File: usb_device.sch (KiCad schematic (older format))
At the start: 9 parts, among them J4 USB_C_Receptacle, U7 USB6B1, U8 USB6B1

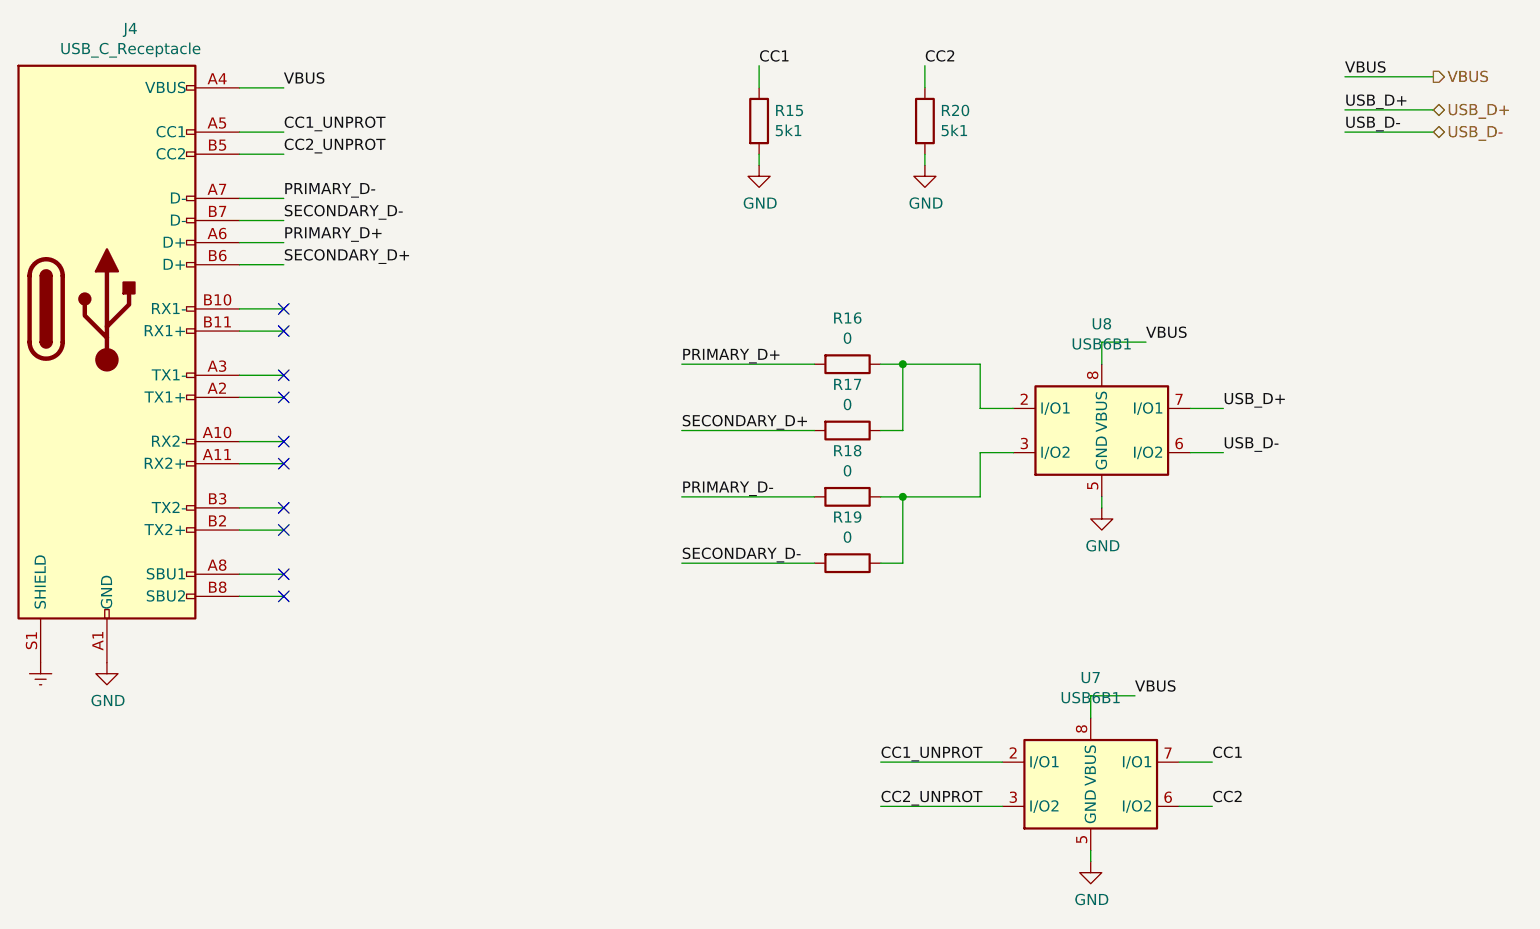
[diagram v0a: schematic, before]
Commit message: Complete muxing and level translation
Added Aux USB to avoid using a HUB, which don't seem to be too readily
available out there and would complicate the design for no good reason.

Now the i2c lines can also be switched.

Added voltage level translation up to 1.2V from 3.3V. Selected
bidirectional level translator.

Started looking into power supply.
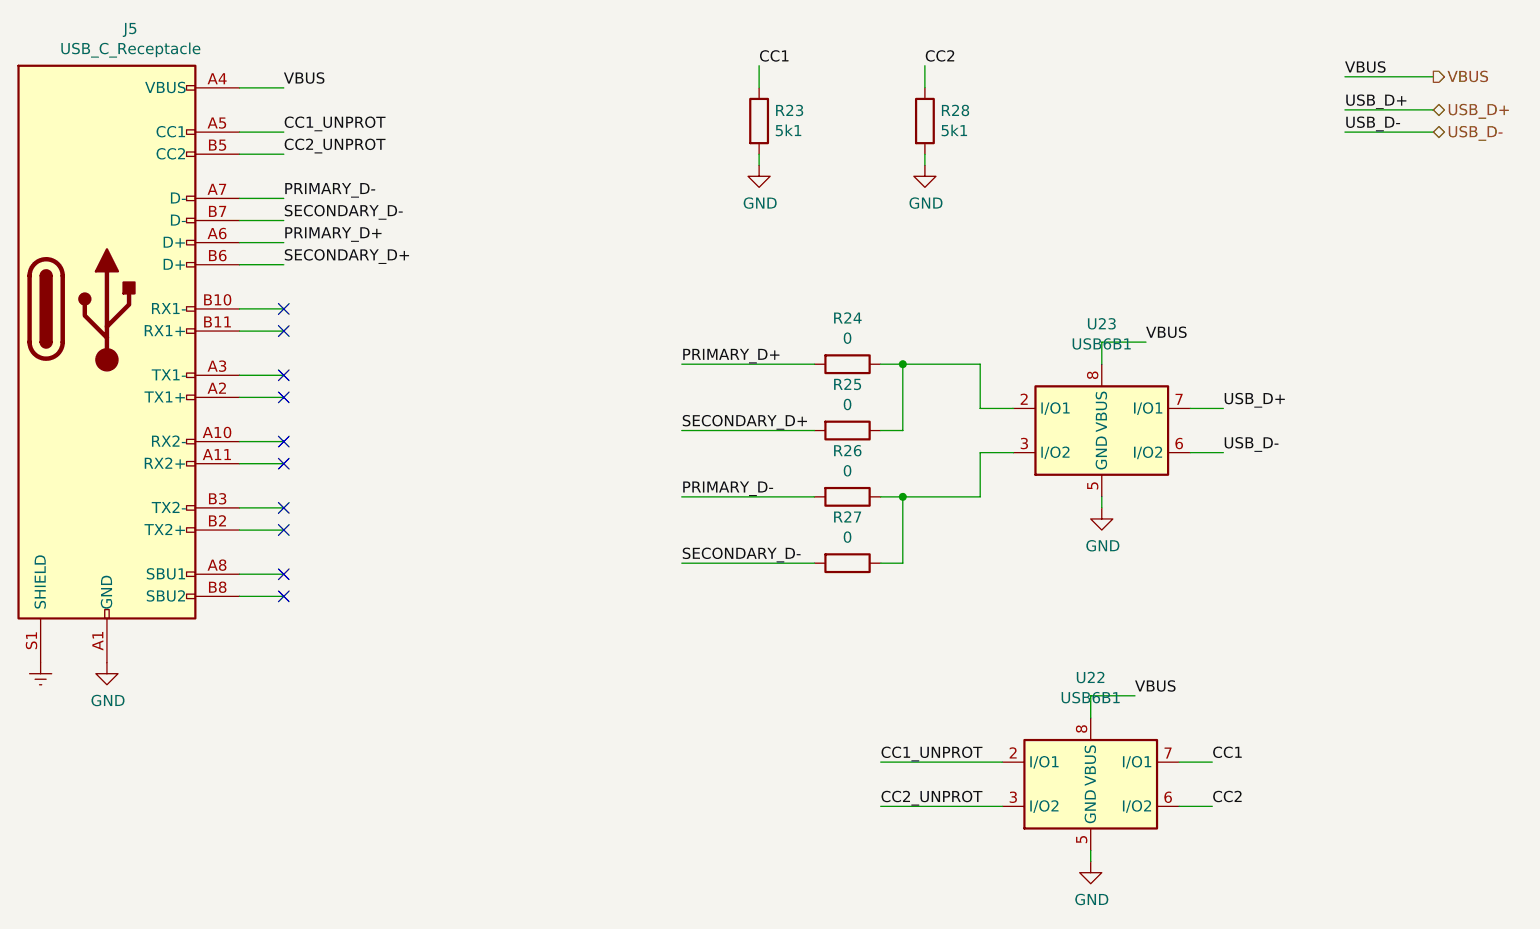
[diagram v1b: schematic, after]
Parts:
- renumbered J4 to J3, R16 to R10, R17 to R11, R18 to R12, R19 to R13, R20 to R14, R15 to R9, U7 to U6, U8 to U7
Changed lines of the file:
@@
 $Descr A4 11693 8268
 encoding utf-8
-Sheet 3 9
+Sheet 12 12
 Title "USB Whisperer"
 Date "2021-11-21"
@@
 P 2600 3000
 AR Path="/61B10DC4" Ref="J?"  Part="1"
-AR Path="/61B0D0F9/61B10DC4" Ref="J4"  Part="1"
-F 0 "J4" H 2707 4267 50  0000 C CNN
+AR Path="/61B0D0F9/61B10DC4" Ref="J3"  Part="1"
+AR Path="/61AFE355/61B10DC4" Ref="J5"  Part="1"
+F 0 "J5" H 2707 4267 50  0000 C CNN
 F 1 "USB_C_Receptacle" H 2707 4176 50  0000 C CNN
 F 2 "" H 2750 3000 50  0001 C CNN
@@
 P 2600 4600
 AR Path="/61B10DD4" Ref="#PWR?"  Part="1"
-AR Path="/61B0D0F9/61B10DD4" Ref="#PWR024"  Part="1"
-F 0 "#PWR024" H 2600 4350 50  0001 C CNN
+AR Path="/61B0D0F9/61B10DD4" Ref="#PWR012"  Part="1"
+AR Path="/61AFE355/61B10DD4" Ref="#PWR062"  Part="1"
+F 0 "#PWR062" H 2600 4350 50  0001 C CNN
 F 1 "GND" H 2605 4427 50  0000 C CNN
 F 2 "" H 2600 4600 50  0001 C CNN
@@
 P 2300 4600
 AR Path="/61B10DDA" Ref="#PWR?"  Part="1"
-AR Path="/61B0D0F9/61B10DDA" Ref="#PWR023"  Part="1"
-F 0 "#PWR023" H 2300 4350 50  0001 C CNN
+AR Path="/61B0D0F9/61B10DDA" Ref="#PWR011"  Part="1"
+AR Path="/61AFE355/61B10DDA" Ref="#PWR061"  Part="1"
+F 0 "#PWR061" H 2300 4350 50  0001 C CNN
 F 1 "Earth" H 2300 4450 50  0001 C CNN
 F 2 "" H 2300 4600 50  0001 C CNN
@@
 	3200 2800 3400 2800
 $Comp
-L Device:R R15
+L Device:R R9
 U 1 1 61B166FB
 P 5550 2150
-F 0 "R15" H 5620 2196 50  0000 L CNN
+AR Path="/61B0D0F9/61B166FB" Ref="R9"  Part="1"
+AR Path="/61AFE355/61B166FB" Ref="R23"  Part="1"
+F 0 "R23" H 5620 2196 50  0000 L CNN
 F 1 "5k1" H 5620 2105 50  0000 L CNN
 F 2 "" V 5480 2150 50  0001 C CNN
@@
 $EndComp
 $Comp
-L Device:R R20
+L Device:R R14
 U 1 1 61B16DA0
 P 6300 2150
-F 0 "R20" H 6370 2196 50  0000 L CNN
+AR Path="/61B0D0F9/61B16DA0" Ref="R14"  Part="1"
+AR Path="/61AFE355/61B16DA0" Ref="R28"  Part="1"
+F 0 "R28" H 6370 2196 50  0000 L CNN
 F 1 "5k1" H 6370 2105 50  0000 L CNN
 F 2 "" V 6230 2150 50  0001 C CNN
@@
 CC2
 $Comp
-L power:GND #PWR025
+L power:GND #PWR013
 U 1 1 61B17220
 P 5550 2350
-F 0 "#PWR025" H 5550 2100 50  0001 C CNN
+AR Path="/61B0D0F9/61B17220" Ref="#PWR013"  Part="1"
+AR Path="/61AFE355/61B17220" Ref="#PWR063"  Part="1"
+F 0 "#PWR063" H 5550 2100 50  0001 C CNN
 F 1 "GND" H 5555 2177 50  0000 C CNN
 F 2 "" H 5550 2350 50  0001 C CNN
@@
 $EndComp
 $Comp
-L power:GND #PWR026
+L power:GND #PWR014
 U 1 1 61B174BC
 P 6300 2350
-F 0 "#PWR026" H 6300 2100 50  0001 C CNN
+AR Path="/61B0D0F9/61B174BC" Ref="#PWR014"  Part="1"
+AR Path="/61AFE355/61B174BC" Ref="#PWR064"  Part="1"
+F 0 "#PWR064" H 6300 2100 50  0001 C CNN
 F 1 "GND" H 6305 2177 50  0000 C CNN
 F 2 "" H 6300 2350 50  0001 C CNN
@@
 	5550 2000 5550 1900
 $Comp
-L Device:R R16
+L Device:R R10
 U 1 1 61B1833D
 P 5950 3250
-F 0 "R16" V 5743 3250 50  0000 C CNN
+AR Path="/61B0D0F9/61B1833D" Ref="R10"  Part="1"
+AR Path="/61AFE355/61B1833D" Ref="R24"  Part="1"
+F 0 "R24" V 5743 3250 50  0000 C CNN
 F 1 "0" V 5834 3250 50  0000 C CNN
 F 2 "" V 5880 3250 50  0001 C CNN
@@
 $EndComp
 $Comp
-L Device:R R17
+L Device:R R11
 U 1 1 61B18B52
 P 5950 3550
-F 0 "R17" V 5743 3550 50  0000 C CNN
+AR Path="/61B0D0F9/61B18B52" Ref="R11"  Part="1"
+AR Path="/61AFE355/61B18B52" Ref="R25"  Part="1"
+F 0 "R25" V 5743 3550 50  0000 C CNN
 F 1 "0" V 5834 3550 50  0000 C CNN
 F 2 "" V 5880 3550 50  0001 C CNN
@@
 	6200 3250 6100 3250
 $Comp
-L Device:R R18
+L Device:R R12
 U 1 1 61B1BA3B
 P 5950 3850
-F 0 "R18" V 5743 3850 50  0000 C CNN
+AR Path="/61B0D0F9/61B1BA3B" Ref="R12"  Part="1"
+AR Path="/61AFE355/61B1BA3B" Ref="R26"  Part="1"
+F 0 "R26" V 5743 3850 50  0000 C CNN
 F 1 "0" V 5834 3850 50  0000 C CNN
 F 2 "" V 5880 3850 50  0001 C CNN
@@
 $EndComp
 $Comp
-L Device:R R19
+L Device:R R13
 U 1 1 61B1BA41
 P 5950 4150
-F 0 "R19" V 5743 4150 50  0000 C CNN
+AR Path="/61B0D0F9/61B1BA41" Ref="R13"  Part="1"
+AR Path="/61AFE355/61B1BA41" Ref="R27"  Part="1"
+F 0 "R27" V 5743 4150 50  0000 C CNN
 F 1 "0" V 5834 4150 50  0000 C CNN
 F 2 "" V 5880 4150 50  0001 C CNN
@@
 	8600 1950 8200 1950
 $Comp
-L Power_Protection:USB6B1 U8
+L Power_Protection:USB6B1 U7
 U 1 1 61B30609
 P 7100 3550
-F 0 "U8" H 7100 4031 50  0000 C CNN
+AR Path="/61B0D0F9/61B30609" Ref="U7"  Part="1"
+AR Path="/61AFE355/61B30609" Ref="U23"  Part="1"
+F 0 "U23" H 7100 4031 50  0000 C CNN
 F 1 "USB6B1" H 7100 3940 50  0000 C CNN
 F 2 "Package_SO:SOIC-8_3.9x4.9mm_P1.27mm" H 7100 3550 50  0001 C CNN
@@
 	6200 3850 6550 3850
 $Comp
-L power:GND #PWR028
+L power:GND #PWR016
 U 1 1 61B36C9F
 P 7100 3900
-F 0 "#PWR028" H 7100 3650 50  0001 C CNN
+AR Path="/61B0D0F9/61B36C9F" Ref="#PWR016"  Part="1"
+AR Path="/61AFE355/61B36C9F" Ref="#PWR066"  Part="1"
+F 0 "#PWR066" H 7100 3650 50  0001 C CNN
 F 1 "GND" H 7105 3727 50  0000 C CNN
 F 2 "" H 7100 3900 50  0001 C CNN
@@
 CC2
 $Comp
-L Power_Protection:USB6B1 U7
+L Power_Protection:USB6B1 U6
 U 1 1 61BB6C09
 P 7050 5150
-F 0 "U7" H 7050 5631 50  0000 C CNN
+AR Path="/61B0D0F9/61BB6C09" Ref="U6"  Part="1"
+AR Path="/61AFE355/61BB6C09" Ref="U22"  Part="1"
+F 0 "U22" H 7050 5631 50  0000 C CNN
 F 1 "USB6B1" H 7050 5540 50  0000 C CNN
 F 2 "Package_SO:SOIC-8_3.9x4.9mm_P1.27mm" H 7050 5150 50  0001 C CNN
@@
 	7600 5250 7450 5250
 $Comp
-L power:GND #PWR027
+L power:GND #PWR015
 U 1 1 61BB6C17
 P 7050 5500
-F 0 "#PWR027" H 7050 5250 50  0001 C CNN
+AR Path="/61B0D0F9/61BB6C17" Ref="#PWR015"  Part="1"
+AR Path="/61AFE355/61BB6C17" Ref="#PWR065"  Part="1"
+F 0 "#PWR065" H 7050 5250 50  0001 C CNN
 F 1 "GND" H 7055 5327 50  0000 C CNN
 F 2 "" H 7050 5500 50  0001 C CNN

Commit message: Add initial power design
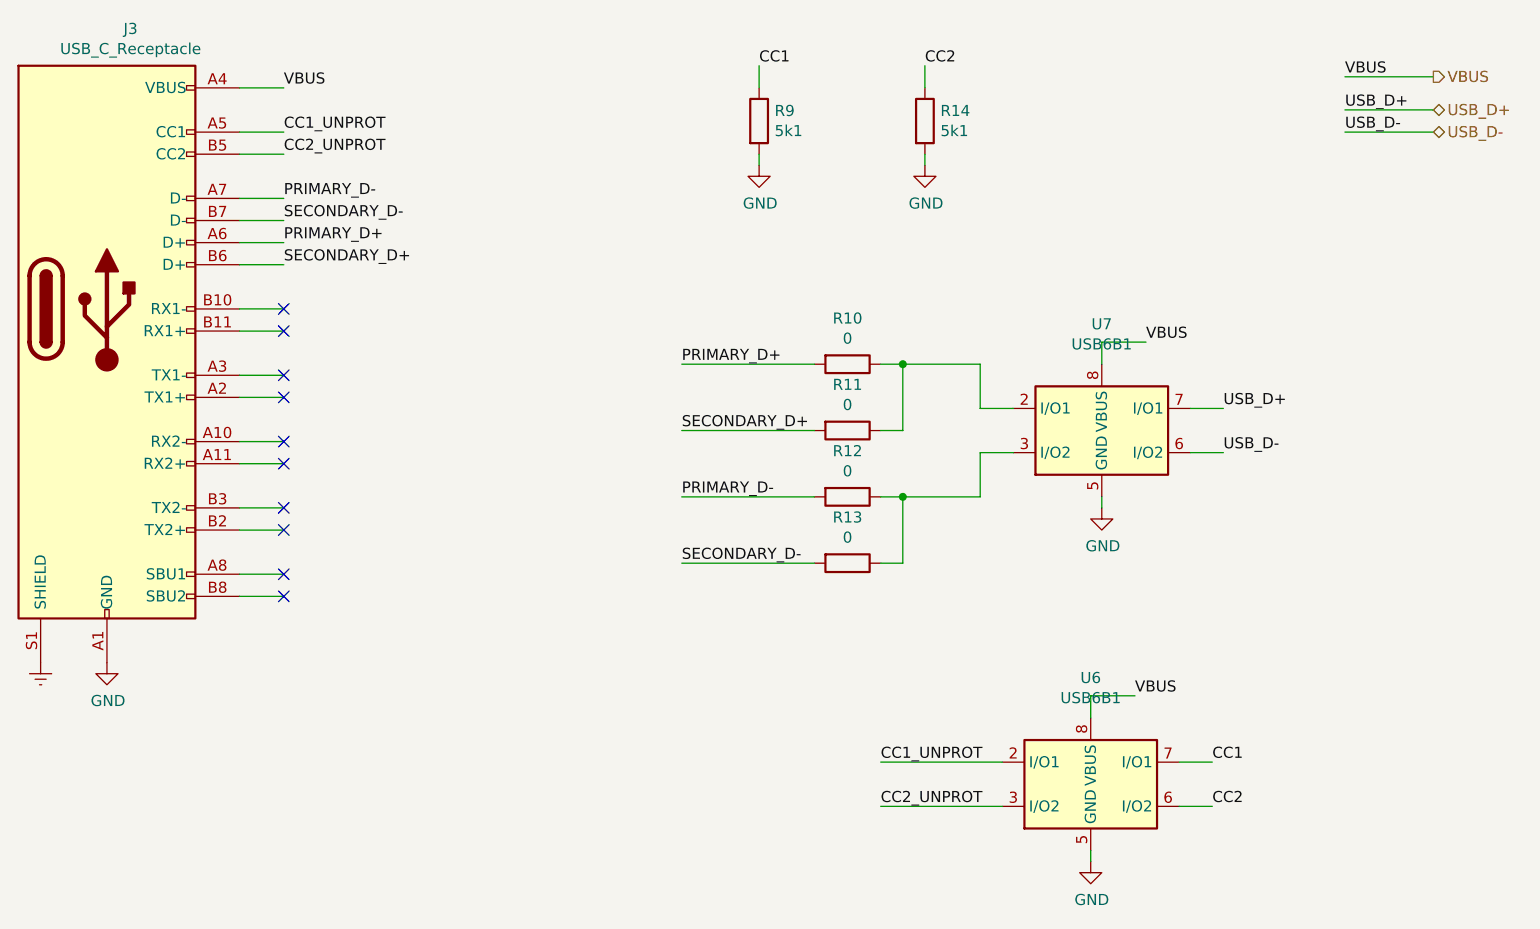
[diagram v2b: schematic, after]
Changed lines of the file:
@@
 $Descr A4 11693 8268
 encoding utf-8
-Sheet 12 12
+Sheet 3 12
 Title "USB Whisperer"
 Date "2021-11-21"
@@
 AR Path="/61B0D0F9/61B10DC4" Ref="J3"  Part="1"
 AR Path="/61AFE355/61B10DC4" Ref="J5"  Part="1"
-F 0 "J5" H 2707 4267 50  0000 C CNN
+F 0 "J3" H 2707 4267 50  0000 C CNN
 F 1 "USB_C_Receptacle" H 2707 4176 50  0000 C CNN
 F 2 "" H 2750 3000 50  0001 C CNN
@@
 AR Path="/61B0D0F9/61B10DD4" Ref="#PWR012"  Part="1"
 AR Path="/61AFE355/61B10DD4" Ref="#PWR062"  Part="1"
-F 0 "#PWR062" H 2600 4350 50  0001 C CNN
+F 0 "#PWR012" H 2600 4350 50  0001 C CNN
 F 1 "GND" H 2605 4427 50  0000 C CNN
 F 2 "" H 2600 4600 50  0001 C CNN
@@
 AR Path="/61B0D0F9/61B10DDA" Ref="#PWR011"  Part="1"
 AR Path="/61AFE355/61B10DDA" Ref="#PWR061"  Part="1"
-F 0 "#PWR061" H 2300 4350 50  0001 C CNN
+F 0 "#PWR011" H 2300 4350 50  0001 C CNN
 F 1 "Earth" H 2300 4450 50  0001 C CNN
 F 2 "" H 2300 4600 50  0001 C CNN
@@
 AR Path="/61B0D0F9/61B166FB" Ref="R9"  Part="1"
 AR Path="/61AFE355/61B166FB" Ref="R23"  Part="1"
-F 0 "R23" H 5620 2196 50  0000 L CNN
+F 0 "R9" H 5620 2196 50  0000 L CNN
 F 1 "5k1" H 5620 2105 50  0000 L CNN
 F 2 "" V 5480 2150 50  0001 C CNN
@@
 AR Path="/61B0D0F9/61B16DA0" Ref="R14"  Part="1"
 AR Path="/61AFE355/61B16DA0" Ref="R28"  Part="1"
-F 0 "R28" H 6370 2196 50  0000 L CNN
+F 0 "R14" H 6370 2196 50  0000 L CNN
 F 1 "5k1" H 6370 2105 50  0000 L CNN
 F 2 "" V 6230 2150 50  0001 C CNN
@@
 AR Path="/61B0D0F9/61B17220" Ref="#PWR013"  Part="1"
 AR Path="/61AFE355/61B17220" Ref="#PWR063"  Part="1"
-F 0 "#PWR063" H 5550 2100 50  0001 C CNN
+F 0 "#PWR013" H 5550 2100 50  0001 C CNN
 F 1 "GND" H 5555 2177 50  0000 C CNN
 F 2 "" H 5550 2350 50  0001 C CNN
@@
 AR Path="/61B0D0F9/61B174BC" Ref="#PWR014"  Part="1"
 AR Path="/61AFE355/61B174BC" Ref="#PWR064"  Part="1"
-F 0 "#PWR064" H 6300 2100 50  0001 C CNN
+F 0 "#PWR014" H 6300 2100 50  0001 C CNN
 F 1 "GND" H 6305 2177 50  0000 C CNN
 F 2 "" H 6300 2350 50  0001 C CNN
@@
 AR Path="/61B0D0F9/61B1833D" Ref="R10"  Part="1"
 AR Path="/61AFE355/61B1833D" Ref="R24"  Part="1"
-F 0 "R24" V 5743 3250 50  0000 C CNN
+F 0 "R10" V 5743 3250 50  0000 C CNN
 F 1 "0" V 5834 3250 50  0000 C CNN
 F 2 "" V 5880 3250 50  0001 C CNN
@@
 AR Path="/61B0D0F9/61B18B52" Ref="R11"  Part="1"
 AR Path="/61AFE355/61B18B52" Ref="R25"  Part="1"
-F 0 "R25" V 5743 3550 50  0000 C CNN
+F 0 "R11" V 5743 3550 50  0000 C CNN
 F 1 "0" V 5834 3550 50  0000 C CNN
 F 2 "" V 5880 3550 50  0001 C CNN
@@
 AR Path="/61B0D0F9/61B1BA3B" Ref="R12"  Part="1"
 AR Path="/61AFE355/61B1BA3B" Ref="R26"  Part="1"
-F 0 "R26" V 5743 3850 50  0000 C CNN
+F 0 "R12" V 5743 3850 50  0000 C CNN
 F 1 "0" V 5834 3850 50  0000 C CNN
 F 2 "" V 5880 3850 50  0001 C CNN
@@
 AR Path="/61B0D0F9/61B1BA41" Ref="R13"  Part="1"
 AR Path="/61AFE355/61B1BA41" Ref="R27"  Part="1"
-F 0 "R27" V 5743 4150 50  0000 C CNN
+F 0 "R13" V 5743 4150 50  0000 C CNN
 F 1 "0" V 5834 4150 50  0000 C CNN
 F 2 "" V 5880 4150 50  0001 C CNN
@@
 AR Path="/61B0D0F9/61B30609" Ref="U7"  Part="1"
 AR Path="/61AFE355/61B30609" Ref="U23"  Part="1"
-F 0 "U23" H 7100 4031 50  0000 C CNN
+F 0 "U7" H 7100 4031 50  0000 C CNN
 F 1 "USB6B1" H 7100 3940 50  0000 C CNN
 F 2 "Package_SO:SOIC-8_3.9x4.9mm_P1.27mm" H 7100 3550 50  0001 C CNN
@@
 AR Path="/61B0D0F9/61B36C9F" Ref="#PWR016"  Part="1"
 AR Path="/61AFE355/61B36C9F" Ref="#PWR066"  Part="1"
-F 0 "#PWR066" H 7100 3650 50  0001 C CNN
+F 0 "#PWR016" H 7100 3650 50  0001 C CNN
 F 1 "GND" H 7105 3727 50  0000 C CNN
 F 2 "" H 7100 3900 50  0001 C CNN
@@
 AR Path="/61B0D0F9/61BB6C09" Ref="U6"  Part="1"
 AR Path="/61AFE355/61BB6C09" Ref="U22"  Part="1"
-F 0 "U22" H 7050 5631 50  0000 C CNN
+F 0 "U6" H 7050 5631 50  0000 C CNN
 F 1 "USB6B1" H 7050 5540 50  0000 C CNN
 F 2 "Package_SO:SOIC-8_3.9x4.9mm_P1.27mm" H 7050 5150 50  0001 C CNN
@@
 AR Path="/61B0D0F9/61BB6C17" Ref="#PWR015"  Part="1"
 AR Path="/61AFE355/61BB6C17" Ref="#PWR065"  Part="1"
-F 0 "#PWR065" H 7050 5250 50  0001 C CNN
+F 0 "#PWR015" H 7050 5250 50  0001 C CNN
 F 1 "GND" H 7055 5327 50  0000 C CNN
 F 2 "" H 7050 5500 50  0001 C CNN
